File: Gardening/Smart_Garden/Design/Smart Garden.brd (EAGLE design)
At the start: 100 x 80 mm, 68 parts, among them IC1 7809DT, IC2 LM1117-3.3, IC3 7805DT, J1 AUDIO_JACK_TRRSSMD_RA, J2 AUDIO_JACK_TRRSSMD_RA, J3 AUDIO_JACK_TRRSSMD_RA, J4 AUDIO_JACK_TRRSSMD_RA, T1 BC847, T2 BC847, T3 BC847, T4 BC847, U1 ESP-32S, U4 MB6S, X1 22-23-2021, X2 22-23-2021, X3 22-23-2021, X4 22-23-2021, X5 22-23-2021

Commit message: Updated Smart Garden Project docomentation
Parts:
- removed X1, X2, X3, X4, X5: 22-23-2021, con-molex:22-23-2021
- added X10, X6, X7, X8, X9: (no value), con-wago-500:W237-102
- moved H1 2.00 mm to (5.00, 3.00)
- moved H2 2.00 mm to (95.0, 3.30)
- moved L2 1.00 mm to (12.0, 6.00)
- moved L3 1.00 mm to (32.0, 6.00)
- moved L4 1.00 mm to (52.0, 6.00)
- moved L5 1.00 mm to (72.0, 6.00)
- moved R12 1.00 mm to (12.0, 6.00)
- moved R13 1.00 mm to (32.0, 6.00)
- moved R14 1.00 mm to (52.0, 6.00)
- moved R15 1.00 mm to (72.0, 6.00)
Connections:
- net 1R1: now also X7.2; no longer X1.1
- net 2R1: now also X8.2; no longer X2.1
- net 3R1: now also X9.2; no longer X3.1
- net 4R1: now also X10.2; no longer X4.1
- net AC1: now also X6.1; no longer X5.2
- net AC2: now also X6.2; no longer X5.1
- net N$1: now also X10.1; no longer X4.2
- net N$2: now also X9.1; no longer X3.2
- net N$4: now also X8.1; no longer X2.2
- net N$5: now also X7.1; no longer X1.2
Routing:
- net IO19: track 75.7 -> 80.7 mm
- net IO17: track 79.6 -> 84.6 mm
- net IO16: track 97.7 -> 102.7 mm
- net IO18: track 62.8 -> 65.4 mm
- net AC1: track 36.3 -> 37.0 mm
- net N$4: track 19.7 -> 19.1 mm
- net N$2: track 20.1 -> 19.5 mm
- net N$1: track 20.5 -> 20.0 mm
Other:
- board size 100 x 80 mm -> 100 x 82 mm

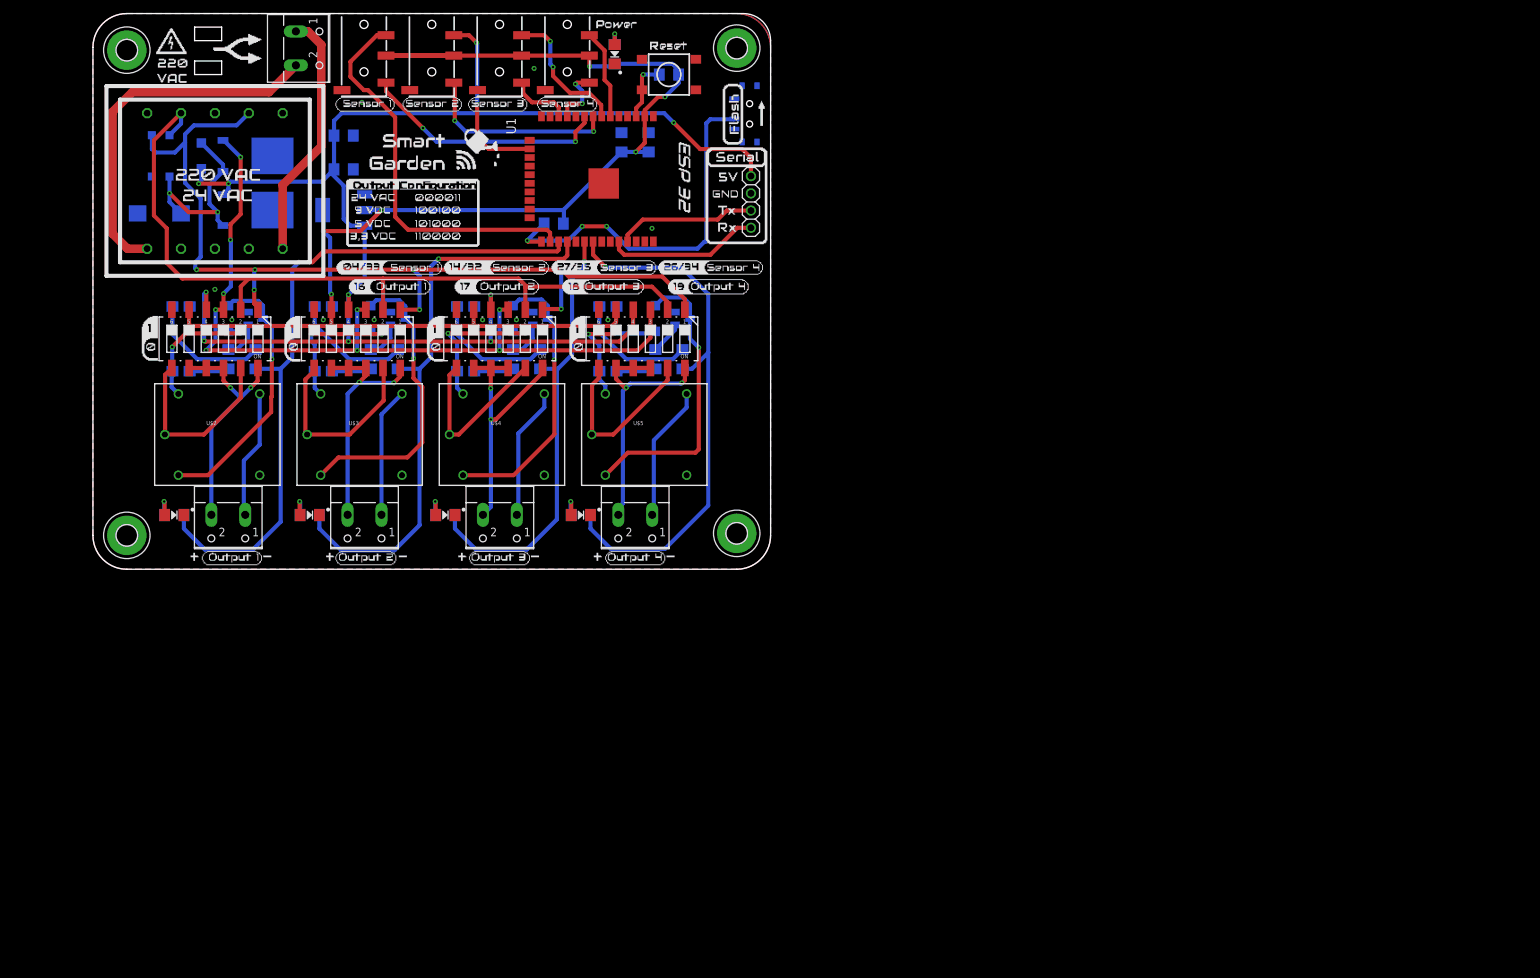
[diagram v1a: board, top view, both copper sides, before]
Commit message: First commit to Smart Garden V1.1.0, changes apply mainly to schematics:  * Relay 5V supply  * Removed 220-24VAC transformator  * Staged power supply regulation with 12V step  * Push-buttons connection pins added
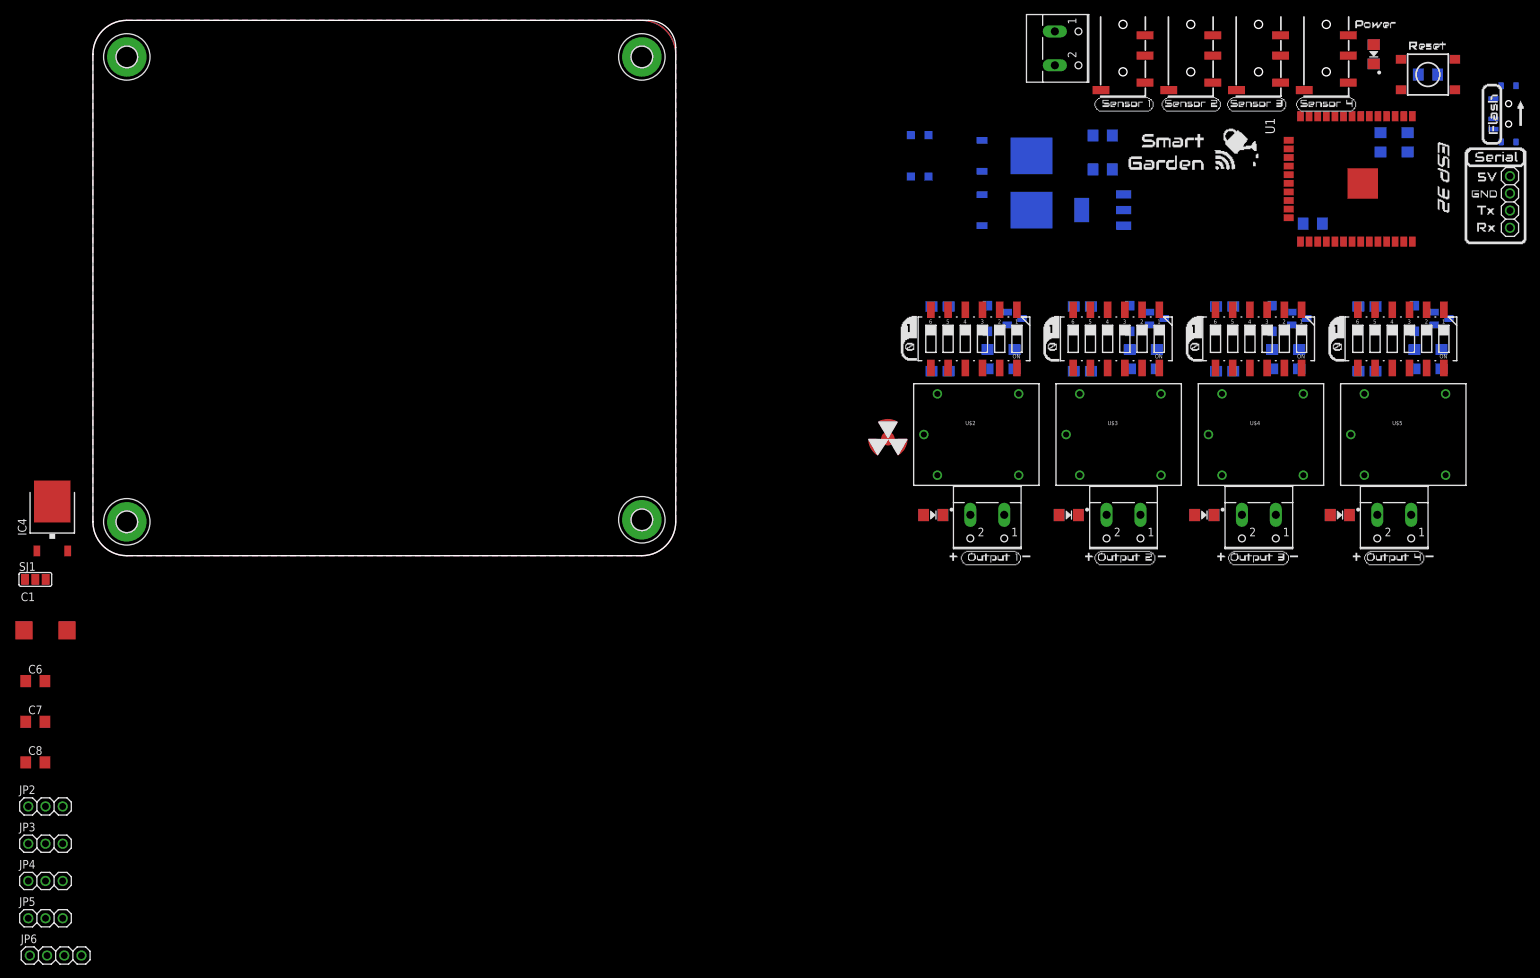
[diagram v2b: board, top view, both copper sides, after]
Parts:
- removed D1: (no value), diode:SOD123
- removed U$1: TRANSFORMADOR_PE3010-M, SpaceDIY_special_components:TRANSFORMADOR_PE3010-M
- added C6, C7, C8: 100nF, SpaceDIY_passive_components:1206
- added IC4: 7812DT, adafruit:TO252
- added JP2, JP3, JP4, JP5: (no value), adafruit:1X03
- added JP6: Power_switch, SpaceDIY_connectors:1X04
- added SJ1: (no value), jumper:SJ_2
- added SJ2: (no value), SpaceDIY_connectors:SJ_3_R
- C1: device resistor:CT7343 -> rcl:D/7343-31R
- moved C2 112.0 mm to (149.0, 62.0)
- moved C3 112.0 mm to (149.0, 57.0)
- moved C4 112.0 mm to (194.0, 61.0)
- moved C5 112.0 mm to (190.0, 61.0)
- moved D2 112.0 mm to (132.0, 35.0)
- moved D3 112.0 mm to (153.0, 35.0)
- moved D4 112.0 mm to (174.0, 35.0)
- moved D5 112.0 mm to (195.0, 35.0)
- moved IC1 112.0 mm to (136.0, 59.0)
- moved IC2 112.0 mm to (149.0, 51.0)
- moved IC3 112.0 mm to (136.0, 51.0)
- moved J1 112.0 mm to (182.0, 80.0)
- moved J2 112.0 mm to (172.0, 80.0)
- moved J3 112.0 mm to (162.0, 80.0)
- moved J4 112.0 mm to (152.0, 80.0)
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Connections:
- removed net 24VDC: C1.+, D1.C, IC1.1, IC3.1, U4.+
- removed net AC1: U$1.P2, X6.1
- removed net AC2: U$1.P1, X6.2
- removed net N$10: D3.C, OK2.4, U$3.COIL1
- removed net N$14: D4.C, OK3.4, U$4.COIL1
- removed net N$18: D5.C, OK4.4, U$5.COIL1
- new net 12V: C7.1, IC4.2, S2.3, S3.3, S4.3, S5.3, SJ1.1, SJ2.P$4
- new net 24V: C1.+, C6.1, IC4.1, SJ1.3, SJ2.P$3, U4.+
- new net IO3: JP3.3
- new net N$30: IC1.1, SJ1.2
- new net N$32: IC3.1, SJ2.P$1
- net 24V1: now also JP6.3; no longer U$1.S2
- net 24V2: now also X6.2; no longer U$1.S1
- net 3V3: now also JP6.2; no longer S2.5, S3.5, S4.5, S5.5
- net 5V: now also D2.C, D3.C, D4.C, D5.C, OK1.4, OK2.4, OK3.4, OK4.4, S2.5, S3.5, S4.5, S5.5, U$2.COIL1, U$3.COIL1, U$4.COIL1, U$5.COIL1; no longer D1.A, S2.4, S3.4, S4.4, S5.4
- net 9V: now also C8.1, S2.4, S3.4, S4.4, S5.4, SJ2.P$2; no longer S2.3, S3.3, S4.3, S5.3
- net GND: now also C6.2, C7.2, C8.2, IC4.3, JP2.1, JP3.1, JP4.1, JP5.1, JP6.1
- net IO12: now also JP2.2
- net IO13: now also JP3.2
- net IO15: now also JP5.3
- net IO2: now also JP2.3
- net IO23: now also JP4.2
- net IO25: now also JP5.2
- net IO5: now also JP4.3
- net N$1: now also U$3.SWCLOSED, X8.1; no longer U$5.SWOPEN, X10.1
- net N$2: now also U$2.SWCLOSED, X7.1; no longer U$4.SWOPEN, X9.1
- net N$4: now also U$4.SWCLOSED, X9.1; no longer U$3.SWOPEN, X8.1
- net N$5: now also U$5.SWCLOSED, X10.1; no longer U$2.SWOPEN, X7.1
- net N$6: now also JP6.4, X6.1; no longer D2.C, OK1.4, U$2.COIL1
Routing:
- net 5V: track 217.2 -> 0.00 mm, vias 9 -> 0
- net 3V3: track 215.4 -> 0.00 mm, vias 6 -> 0
- net 24V1: track 139.3 -> 0.00 mm, vias 7 -> 0
- net 9V: track 120.0 -> 0.00 mm, vias 9 -> 0
- net 24V2: track 119.1 -> 0.00 mm
- net IO16: track 102.7 -> 0.00 mm, vias 1 -> 0
- net IO17: track 84.6 -> 0.00 mm, vias 1 -> 0
- net IO19: track 80.7 -> 0.00 mm, vias 1 -> 0
- net IO18: track 65.4 -> 0.00 mm, vias 1 -> 0
- net IO4: track 58.0 -> 0.00 mm
- net IO0: track 56.6 -> 0.00 mm, vias 3 -> 0
- net AC2: track 53.9 -> 0.00 mm
- net N$11: track 43.9 -> 0.00 mm, vias 1 -> 0
- net N$19: track 43.3 -> 0.00 mm, vias 1 -> 0
- net 3R1: track 43.3 -> 0.00 mm, vias 2 -> 0
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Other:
- board size 100 x 82 mm -> 86 x 79 mm

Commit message: Updated Design files
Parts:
- moved JP1 208.8 mm to (3.60, 15.4)
- moved J1 178.4 mm to (12.0, 26.0), turned to 0 degrees
- moved C4 173.2 mm to (21.0, 53.0), turned to 270 degrees
- moved C5 172.2 mm to (18.0, 53.0), turned to 270 degrees
- moved R10 165.9 mm to (35.0, 4.00), turned to 90 degrees
- moved R9 161.9 mm to (18.0, 4.00), turned to 90 degrees
- moved D5 161.2 mm to (35.0, 15.0), turned to 0 degrees
- moved T4 160.1 mm to (40.0, 16.0), turned to 0 degrees
- moved U1 158.1 mm to (30.3, 40.6), flipped to the bottom
- moved R6 158.0 mm to (39.0, 4.00)
- moved D4 157.3 mm to (18.0, 15.0), turned to 0 degrees
- moved T3 156.2 mm to (23.0, 16.0), turned to 0 degrees
- moved U$5 156.2 mm to (37.0, 11.0), turned to 270 degrees
- moved J2 154.7 mm to (24.0, 35.0), turned to 0 degrees
- moved R5 154.0 mm to (22.0, 4.00)
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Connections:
- removed net IO3: JP3.3
- net 1R1: now also X7.1; no longer X7.2
- net 2R1: now also X8.1; no longer X8.2
- net IO13: no longer J3.RING2
- net IO14: now also J3.RING2
- net N$1: now also X8.2; no longer X8.1
- net N$2: now also X7.2; no longer X7.1
- net RX: now also JP3.3
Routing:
- net 3V3: track 0.00 -> 230.0 mm, vias 0 -> 10
- net 5V: track 0.00 -> 214.4 mm, vias 0 -> 14
- net IO25: track 0.00 -> 132.9 mm, vias 0 -> 3
- net IO16: track 0.00 -> 131.1 mm, vias 0 -> 6
- net 24V2: track 0.00 -> 115.3 mm, vias 0 -> 1
- net IO19: track 0.00 -> 111.1 mm, vias 0 -> 5
- net IO18: track 0.00 -> 110.0 mm, vias 0 -> 8
- net IO13: track 0.00 -> 105.2 mm, vias 0 -> 4
- net 12V: track 0.00 -> 99.0 mm, vias 0 -> 5
- net RX: track 0.00 -> 98.7 mm, vias 0 -> 2
- net IO17: track 0.00 -> 93.5 mm, vias 0 -> 5
- net IO15: track 0.00 -> 93.0 mm
- net N$2: track 0.00 -> 88.5 mm, vias 0 -> 3
- net IO0: track 0.00 -> 83.6 mm, vias 0 -> 2
- net N$4: track 0.00 -> 79.1 mm, vias 0 -> 3
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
